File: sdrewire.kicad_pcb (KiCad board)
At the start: 4 copper layers, 31 x 23.6 mm, 98 parts, among them J1 USB_C_Receptacle, J2 Conn_01x06, J3 Micro_SD_Card, J4 Conn_01x08, Q1 DMG1032UV, Q2 BSS84, Q3 DMG1032UV, U1 MIC5363-3.3YMT, U11 SN74LVC1G14DRL, U12 TS3DDR4000ZBAR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

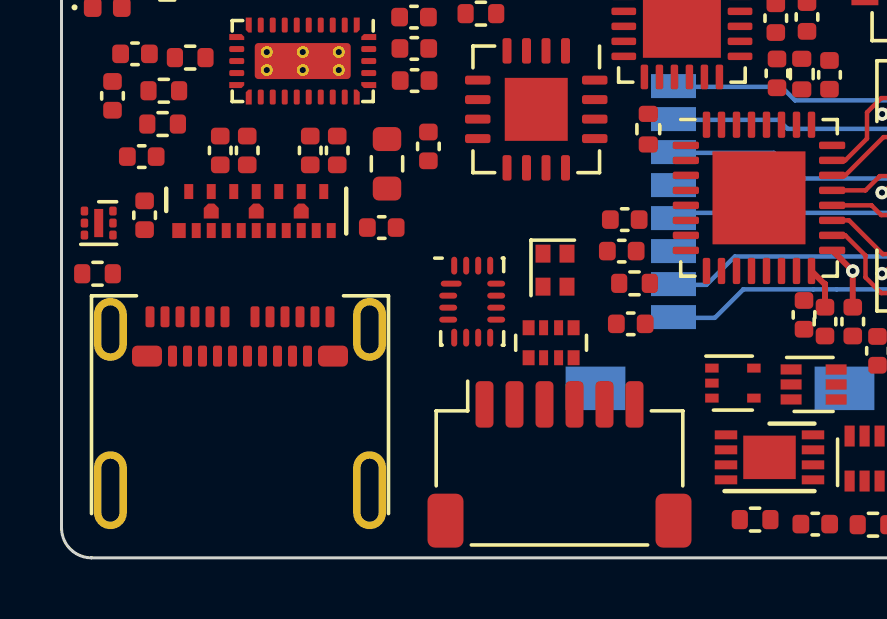
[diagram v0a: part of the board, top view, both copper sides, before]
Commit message: SDReWire: add configurable link for gpio dir
Signed-off-by: Dominik Sliwa <dominik@sliwa.io>
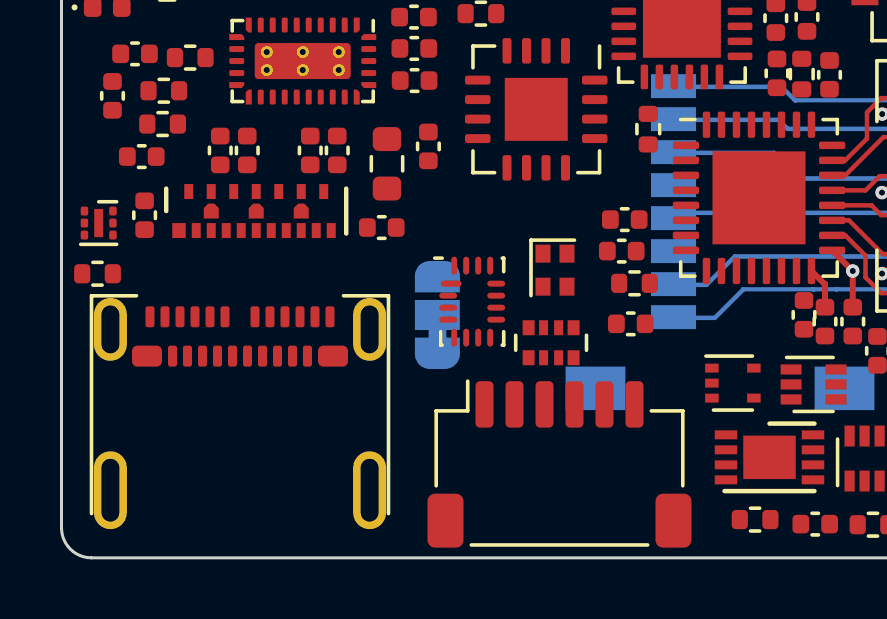
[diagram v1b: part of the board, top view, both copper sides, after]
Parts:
- added JP1: Jumper_3_Bridged12, Jumper:SolderJumper-3_P1.3mm_Bridged12_RoundedPad1.0x1.5mm_NumberLabels, B.Cu at (130.8, 99.6)
- J4: value Conn_01x08 -> uSD_edge_contacts
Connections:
- U5 pad 16: /FTDI/FTDI_V_{DD} -> (no net)
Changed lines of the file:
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@@
   (net 103 "Net-(Q3-Pad2)")
   (net 104 "Net-(RN1-Pad5)")
+  (net 105 "Net-(U5-Pad16)")
   (footprint "Resistor_SMD:R_0402_1005Metric" (layer "F.Cu")
     (at 124.02 86.125)
@@
       (effects (font (size 0.5 0.5) (thickness 0.1)))
     )
-    (fp_text value "Conn_01x08" (at 3.64 -2.55 90) (layer "F.Fab") hide
+    (fp_text value "uSD_edge_contacts" (at 3.64 -2.55 90) (layer "F.Fab") hide
       (effects (font (size 0.3 0.3) (thickness 0.07)))
     )
@@
       (net 2 "GND") (pinfunction "DIR1"))
     (pad "16" smd oval (at -0.6 -1.2) (size 0.2 0.6) (layers "F.Cu" "F.Paste" "F.Mask")
-      (net 32 "/FTDI/FTDI_V_{DD}") (pinfunction "DIR2"))
+      (pinfunction "DIR2"))
     (model "/home/dsliwa/Nextcloud/Projects/Custom.3dshapes/UQFN-16.step"
       (offset (xyz 0 0 0))
@@
     )
   )
+  (footprint "Jumper:SolderJumper-3_P1.3mm_Bridged12_RoundedPad1.0x1.5mm_NumberLabels" (layer "B.Cu")
+    (at 130.83 99.6 90)
+    (descr "SMD Solder 3-pad Jumper, 1x1.5mm rounded Pads, 0.3mm gap, pads 1-2 bridged with 1 copper strip, labeled with numbers")
+    (tags "solder jumper open")
+    (property "Sheet file" "ftdi.kicad_sch")
+    (property "Sheet name" "FTDI")
+    (attr exclude_from_pos_files)
+    (fp_text reference "JP1" (at 0 1.8 90) (layer "B.SilkS")
+      (effects (font (size 1 1) (thickness 0.15)) (justify mirror))
+    )
+    (fp_text value "Jumper_3_Bridged12" (at 0 -1.9 90) (layer "B.Fab")
+      (effects (font (size 1 1) (thickness 0.15)) (justify mirror))
+    )
+    (fp_text user "3" (at 2.6 0 90) (layer "B.SilkS")
+      (effects (font (size 1 1) (thickness 0.15)) (justify mirror))
+    )
+    (fp_text user "1" (at -2.6 0 90) (layer "B.SilkS")
+      (effects (font (size 1 1) (thickness 0.15)) (justify mirror))
+    )
+    (fp_poly (pts (xy -0.9 0.3)
+      (xy -0.4 0.3)
+      (xy -0.4 -0.3)
+      (xy -0.9 -0.3)) (layer "B.Cu") (width 0) (fill solid))
+    (fp_line (start -1.4 1) (end 1.4 1) (layer "B.SilkS") (width 0.12))
+    (fp_line (start 2.05 0.3) (end 2.05 -0.3) (layer "B.SilkS") (width 0.12))
+    (fp_line (start -2.05 -0.3) (end -2.05 0.3) (layer "B.SilkS") (width 0.12))
+    (fp_line (start 1.4 -1) (end -1.4 -1) (layer "B.SilkS") (width 0.12))
+    (fp_arc (start 1.35 -0.3) (end 1.35 -1) (angle 90) (layer "B.SilkS") (width 0.12))
+    (fp_arc (start -1.35 -0.3) (end -2.05 -0.3) (angle 90) (layer "B.SilkS") (width 0.12))
+    (fp_arc (start -1.35 0.3) (end -1.35 1) (angle 90) (layer "B.SilkS") (width 0.12))
+    (fp_arc (start 1.35 0.3) (end 2.05 0.3) (angle 90) (layer "B.SilkS") (width 0.12))
+    (fp_line (start 2.3 -1.25) (end 2.3 1.25) (layer "B.CrtYd") (width 0.05))
+    (fp_line (start -2.3 1.25) (end -2.3 -1.25) (layer "B.CrtYd") (width 0.05))
+    (fp_line (start -2.3 1.25) (end 2.3 1.25) (layer "B.CrtYd") (width 0.05))
+    (fp_line (start 2.3 -1.25) (end -2.3 -1.25) (layer "B.CrtYd") (width 0.05))
+    (pad "1" smd custom (at -1.3 0 90) (size 1 0.5) (layers "B.Cu" "B.Mask")
+      (net 32 "/FTDI/FTDI_V_{DD}") (pinfunction "A") (zone_connect 2)
+      (options (clearance outline) (anchor rect))
+      (primitives
+        (gr_poly (pts
+          (xy 0.55 0.75)
+          (xy 0 0.75)
+          (xy 0 -0.75)
+          (xy 0.55 -0.75)
+        )         (width 0)         (fill yes)        )
+        (gr_circle (center 0 -0.25) (end 0.5 -0.25)         (width 0)         (fill yes)        )
+        (gr_circle (center 0 0.25) (end 0.5 0.25)         (width 0)         (fill yes)        )
+      ))
+    (pad "2" smd rect (at 0 0 90) (size 1 1.5) (layers "B.Cu" "B.Mask")
+      (net 105 "Net-(U5-Pad16)") (pinfunction "C"))
+    (pad "3" smd custom (at 1.3 0 90) (size 1 0.5) (layers "B.Cu" "B.Mask")
+      (net 2 "GND") (pinfunction "B") (zone_connect 2)
+      (options (clearance outline) (anchor rect))
+      (primitives
+        (gr_circle (center 0 -0.25) (end 0.5 -0.25)         (width 0)         (fill yes)        )
+        (gr_circle (center 0 0.25) (end 0.5 0.25)         (width 0)         (fill yes)        )
+        (gr_poly (pts
+          (xy -0.55 0.75)
+          (xy 0 0.75)
+          (xy 0 -0.75)
+          (xy -0.55 -0.75)
+        )         (width 0)         (fill yes)        )
+      ))
+  )
   (footprint "Fiducial:Fiducial_0.5mm_Mask1mm" (layer "B.Cu")

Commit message: SDReWire: fix MIC5363 symbol
Signed-off-by: Dominik Sliwa <dominik@sliwa.io>
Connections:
- JP1 pad 2: Net-(U5-Pad16) -> Net-(JP1-Pad2)
- R37 pad 1: /SD_MUX_SEL -> GND
- R37 pad 2: GND -> /SD_MUX_SEL
- U5 pad 16: (no net) -> /FTDI/FTDI_V_{DD}
- U5 pad 5: /FTDI/FTDI_V_{DD} -> Net-(JP1-Pad2)
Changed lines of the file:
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@@
   (net 103 "Net-(Q3-Pad2)")
   (net 104 "Net-(RN1-Pad5)")
-  (net 105 "Net-(U5-Pad16)")
+  (net 105 "Net-(JP1-Pad2)")
   (footprint "Resistor_SMD:R_0402_1005Metric" (layer "F.Cu")
     (at 124.02 86.125)
@@
     (fp_line (start -0.525 0.27) (end -0.525 -0.27) (layer "F.Fab") (width 0.1))
     (pad "1" smd roundrect (at -0.51 0 180) (size 0.54 0.64) (layers "F.Cu" "F.Paste" "F.Mask") (roundrect_rratio 0.25)
-      (net 75 "/SD_MUX_SEL"))
-    (pad "2" smd roundrect (at 0.51 0 180) (size 0.54 0.64) (layers "F.Cu" "F.Paste" "F.Mask") (roundrect_rratio 0.25)
       (net 2 "GND"))
+    (pad "2" smd roundrect (at 0.51 0 180) (size 0.54 0.64) (layers "F.Cu" "F.Paste" "F.Mask") (roundrect_rratio 0.25)
+      (net 75 "/SD_MUX_SEL"))
     (model "${KISYS3DMOD}/Resistor_SMD.3dshapes/R_0402_1005Metric.wrl"
       (offset (xyz 0 0 0))
@@
       (net 91 "/FTDI/FT_CBUS1") (pinfunction "A4"))
     (pad "5" smd oval (at -0.6 1.2) (size 0.2 0.6) (layers "F.Cu" "F.Paste" "F.Mask")
-      (net 32 "/FTDI/FTDI_V_{DD}") (pinfunction "DIR3"))
+      (net 105 "Net-(JP1-Pad2)") (pinfunction "DIR3"))
     (pad "6" smd oval (at -0.2 1.2) (size 0.2 0.6) (layers "F.Cu" "F.Paste" "F.Mask")
       (net 73 "/FTDI/FT_CBUS2") (pinfunction "DIR4"))
@@
       (net 2 "GND") (pinfunction "DIR1"))
     (pad "16" smd oval (at -0.6 -1.2) (size 0.2 0.6) (layers "F.Cu" "F.Paste" "F.Mask")
-      (pinfunction "DIR2"))
+      (net 32 "/FTDI/FTDI_V_{DD}") (pinfunction "DIR2"))
     (model "/home/dsliwa/Nextcloud/Projects/Custom.3dshapes/UQFN-16.step"
       (offset (xyz 0 0 0))
@@
       ))
     (pad "2" smd rect (at 0 0 90) (size 1 1.5) (layers "B.Cu" "B.Mask")
-      (net 105 "Net-(U5-Pad16)") (pinfunction "C"))
+      (net 105 "Net-(JP1-Pad2)") (pinfunction "C"))
     (pad "3" smd custom (at 1.3 0 90) (size 1 0.5) (layers "B.Cu" "B.Mask")
       (net 2 "GND") (pinfunction "B") (zone_connect 2)

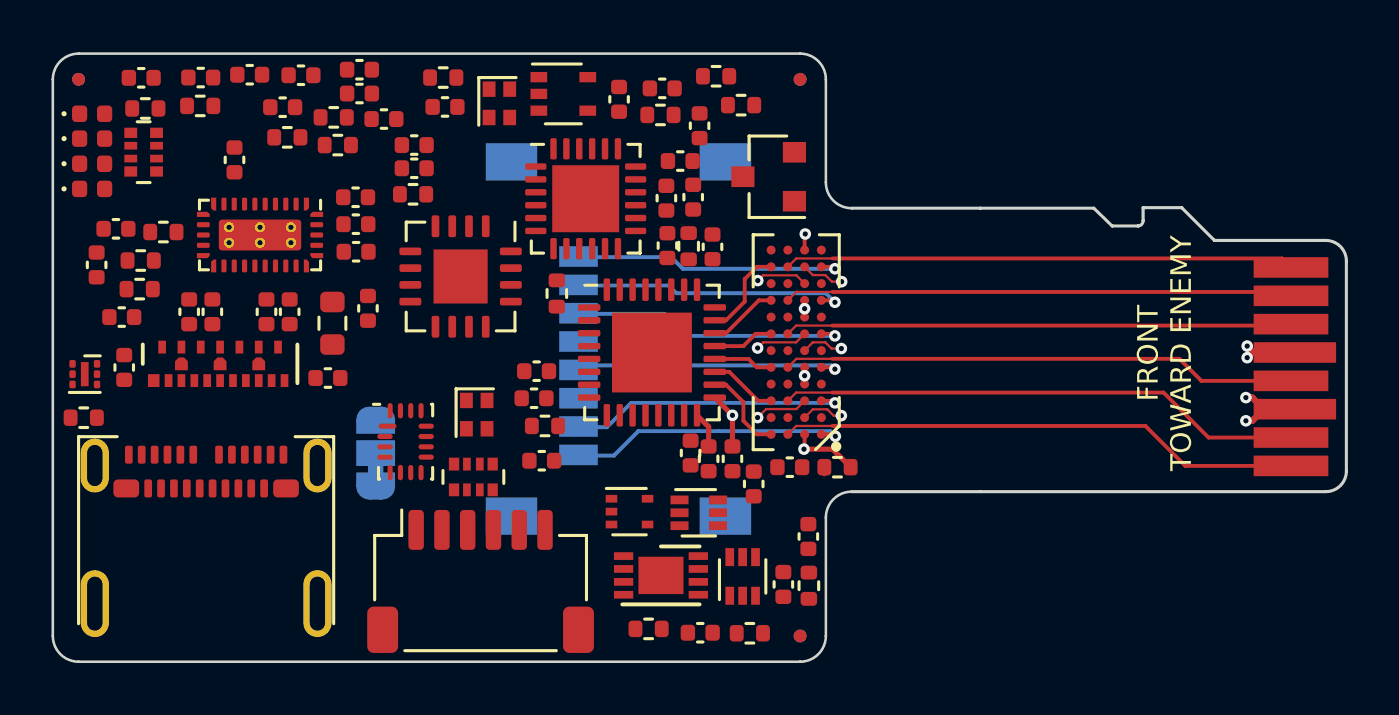
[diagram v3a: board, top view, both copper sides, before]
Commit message: sdrewire: pcb v1
Some itra-pair inversions for easier routing.
Fixed crystal pinouts
sd power p-fet changed for smaller package

Signed-off-by: Dominik Sliwa <dominik@sliwa.io>
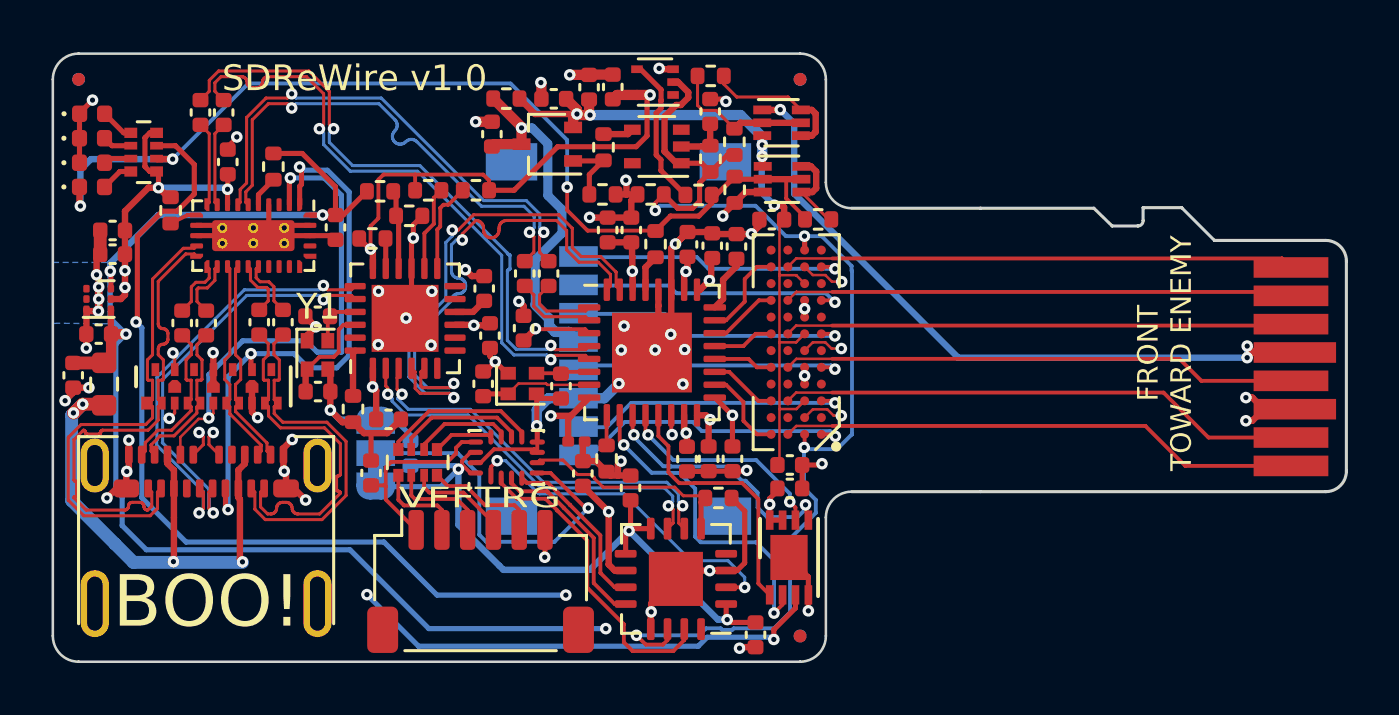
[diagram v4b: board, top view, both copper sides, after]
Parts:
- C48: footprint Capacitor_SMD:C_0402_1005Metric -> Capacitor_SMD:C_0201_0603Metric
- C58: moved to B.Cu
- Q2: value BSS84 -> DMG1013UW; footprint Package_TO_SOT_SMD:SOT-23 -> Package_TO_SOT_SMD:SOT-323_SC-70
- moved R10 26.5 mm to (148.0, 90.5)
- moved C48 20.3 mm to (138.6, 99.2), turned to 180 degrees
- moved C44 18.6 mm to (143.8, 86.3), turned to 90 degrees
- moved R26 17.2 mm to (144.8, 89.4), turned to -90 degrees
- moved C62 17.1 mm to (130.7, 100.4), turned to 90 degrees
- moved R28 17.0 mm to (143.8, 88.2), turned to 90 degrees
- moved R24 17.0 mm to (143.4, 89.6), turned to 0 degrees
- moved U11 16.7 mm to (141.7, 85.2), turned to 180 degrees
- moved Q1 15.5 mm to (146.6, 89.0), turned to 0 degrees
- moved Q3 15.5 mm to (146.6, 86.8)
- moved U7 14.4 mm to (142.5, 104.5), turned to 180 degrees
- moved C15 14.0 mm to (128.6, 97.2), turned to 180 degrees
- moved C20 13.9 mm to (135.0, 96.9), turned to -90 degrees
- moved C58 13.4 mm to (132.2, 99.6)
- moved R25 13.2 mm to (144.8, 87.5), turned to 90 degrees
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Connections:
- net Net-(C14-Pad1) renamed /USB-C/C_USB3_RX-
- C12 pad 2: /GL_USB3_RX- -> /GL_USB3_RX+
- C14 pad 2: /GL_USB3_RX+ -> /GL_USB3_RX-
- J3 pad 9: GND -> (no net)
- RN1 pad 2: Net-(D4-Pad2) -> Net-(D2-Pad2)
- RN1 pad 3: Net-(D3-Pad2) -> Net-(D4-Pad2)
- RN1 pad 4: Net-(D2-Pad2) -> Net-(D3-Pad2)
- RN1 pad 5: Net-(RN1-Pad5) -> +3V3
- RN1 pad 6: +3V3 -> /SD/~SD_MUX_SEL
- RN1 pad 7: /SD/~SD_MUX_SEL -> Net-(RN1-Pad7)
- RN1 pad 8: +5V -> +3V3
- U1 pad 1: +5V -> (no net)
- U1 pad 2: GND -> (no net)
- U1 pad 3: +5V -> GND
- U1 pad 4: (no net) -> +5V
- U1 pad 6: (no net) -> +5V
- U1 pad 7: (no net) -> GND
- U13 pad 3: GND -> (no net)
- U13 pad 5: /SD/SD_{MUX}_V_{DD} -> (no net)
- U14 pad 14: Net-(RN1-Pad5) -> Net-(RN1-Pad7)
- U2 pad 6: /USB-C/C_USB3_TX+ -> /USB-C/C_USB3_TX-
- U2 pad 7: /USB-C/C_USB3_TX- -> /USB-C/C_USB3_TX+
- U3 pad 10: /USB-C/CTX2- -> /USB-C/CTX2+
- U3 pad 11: /USB-C/CTX2+ -> /USB-C/CTX2-
- U3 pad 12: GND -> (no net)
- U3 pad 14: GND -> (no net)
- U3 pad 16: GND -> (no net)
- U3 pad 17: /UFP_USB2_D+ -> /UFP_USB2_D-
- U3 pad 18: GND -> (no net)
- U3 pad 19: GND -> (no net)
- U3 pad 3: /UFP_USB2_D- -> /UFP_USB2_D+
- U3 pad 4: /USB-C/CTX1- -> /USB-C/CTX1+
- U3 pad 5: /USB-C/CTX1+ -> /USB-C/CTX1-
- Y1 pad 1: Net-(C15-Pad2) -> GND
- Y1 pad 2: GND -> Net-(C15-Pad2)
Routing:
- net +3V3: track 0.00 -> 103.6 mm, vias 0 -> 11
- net GND: track 9.27 -> 106.5 mm, vias 7 -> 60
- net +5V: track 0.00 -> 70.4 mm, vias 0 -> 6
- net Net-(RN1-Pad7): track 0.00 -> 47.6 mm, vias 0 -> 3
- net /SD_MUX_SEL: track 3.32 -> 45.2 mm, vias 2 -> 4
- net /SD/~SD_MUX_SEL: track 0.00 -> 39.1 mm, vias 0 -> 3
- net /FTDI/FTDI_V_{DD}: track 0.00 -> 27.3 mm, vias 0 -> 3
- net /SD/EXT_V_{DD}: track 3.89 -> 28.7 mm, vias 2 -> 3
- net Net-(C47-Pad2): track 1.42 -> 25.4 mm, vias 0 -> 4
- net /GL_USB3_RX+: track 0.00 -> 23.9 mm, vias 0 -> 2
- net /GL_USB3_RX-: track 0.00 -> 23.9 mm, vias 0 -> 2
- net /SD/SD_{MUX}_V_{DD}: track 6.18 -> 29.6 mm, vias 3 -> 5
- net /USB-C/CC2: track 0.00 -> 22.3 mm, vias 0 -> 3
- net /UFP_USB2_D-: track 0.00 -> 21.8 mm, vias 0 -> 4
- net /USB-C/V_{BUS}: track 0.00 -> 21.5 mm, vias 0 -> 4
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- added copper zone on B.Cu, net GND
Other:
- board text added: "BOO!"
- board text added: "POWER USB µSD ACT µSD <-> USB µSD <-> DUT"
- board text added: "SDReWire v1.0"
- board text added: "VFFTRG"
- board text added: "dominik@sliwa.io @randomplum"
- board text removed: "SDReWire v1.0 dominik@sliwa.io @randomplum"
